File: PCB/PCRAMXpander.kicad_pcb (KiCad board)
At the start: 2 copper layers, 134.6 x 97.8 mm, 22 parts, among them J1 Bus_ISA_16bit, U1 ATF16V8B-15PU, U2 SN74LVCR16245ADGGR, U3 SN74LVC16244ADGGR, U4 SN74LVC16244ADGGR, U5 AS6C3216A-55TIN, U6 AS6C3216A-55TIN

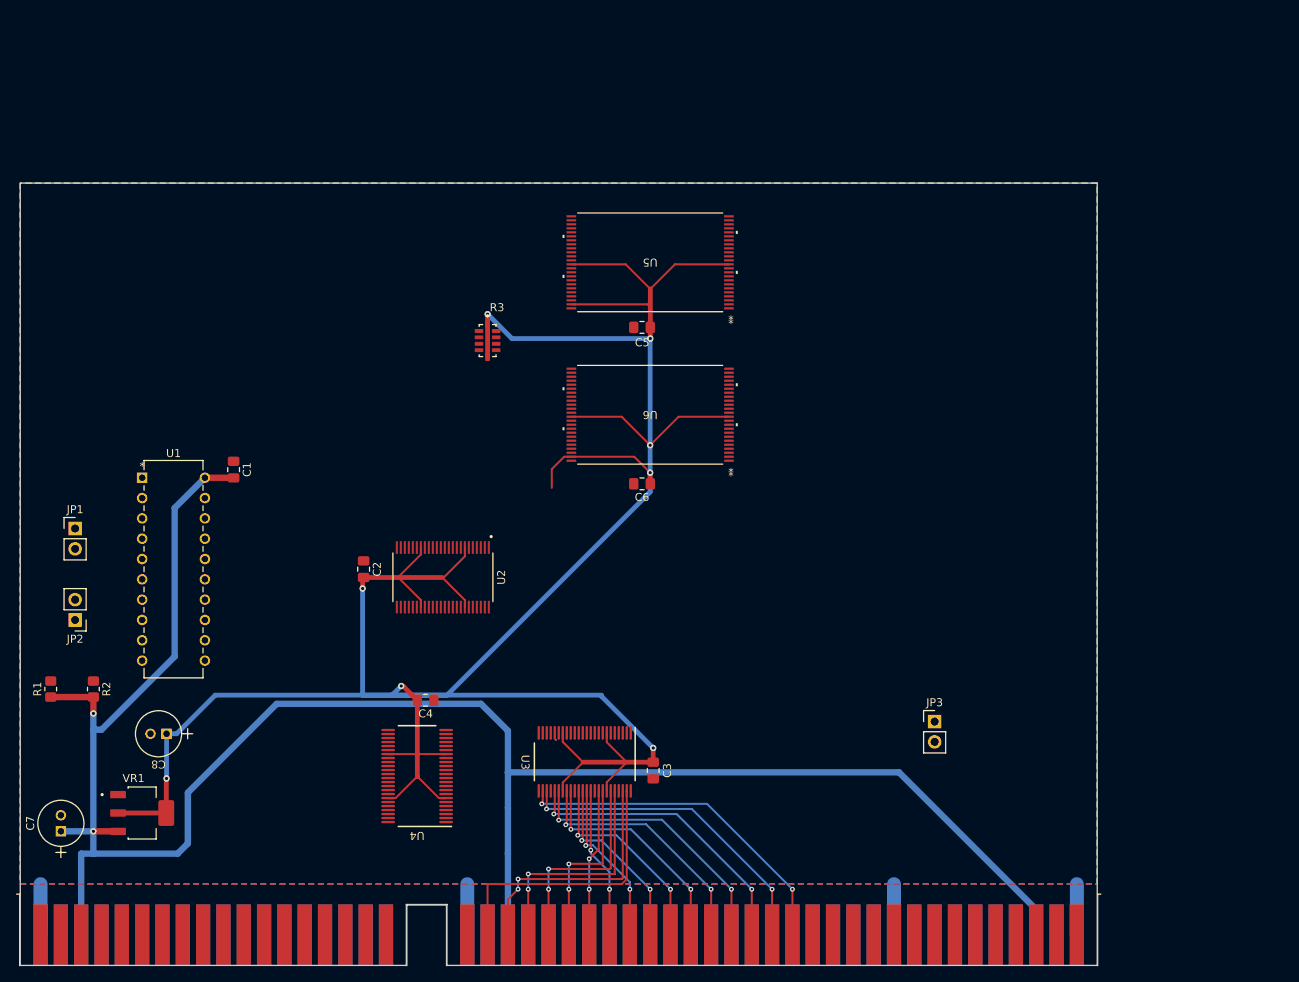
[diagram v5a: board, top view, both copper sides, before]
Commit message: More manual routing
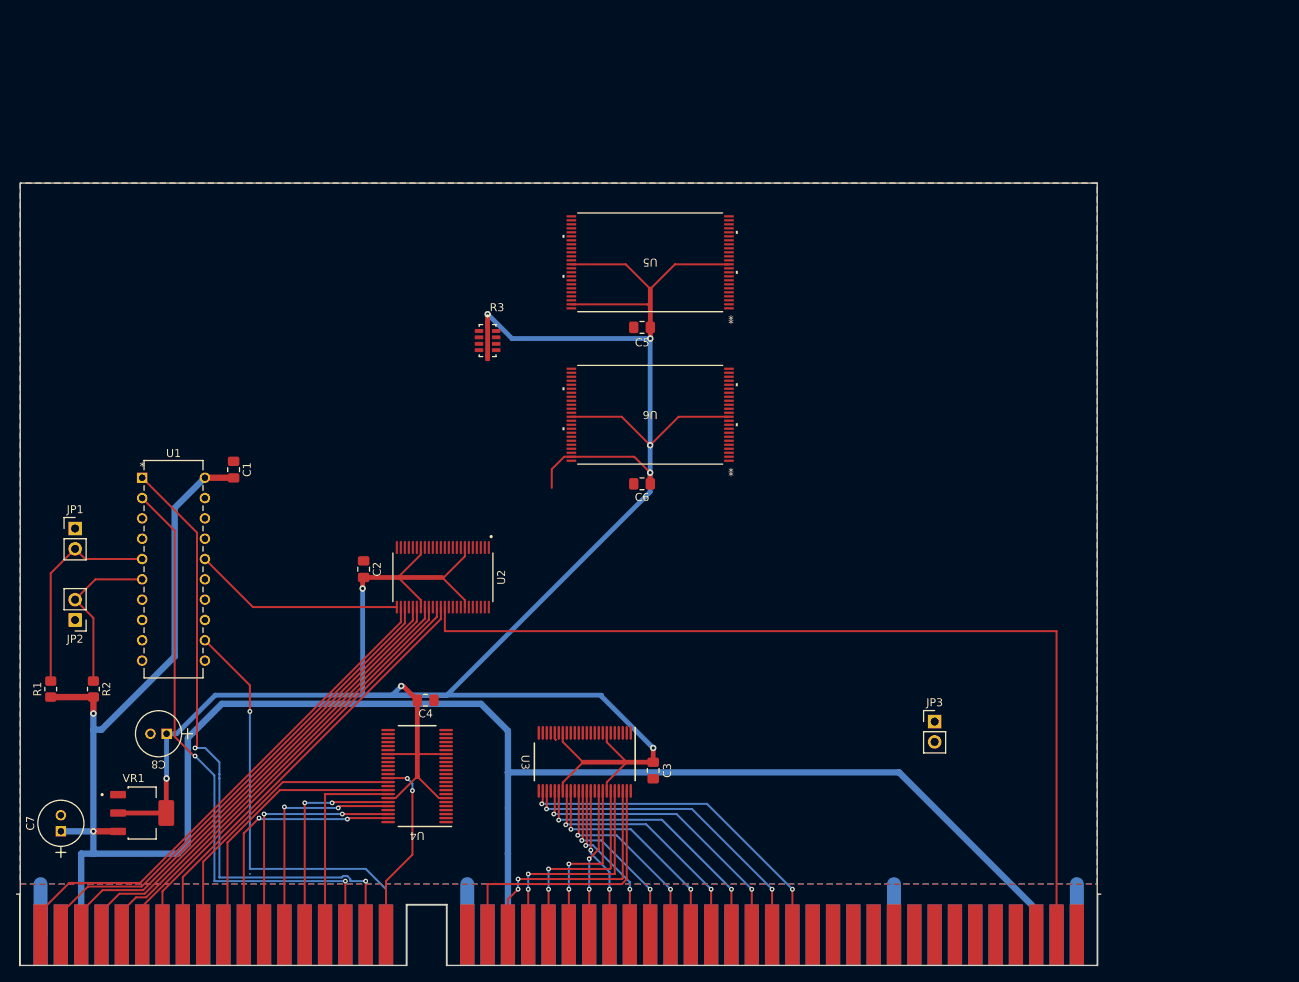
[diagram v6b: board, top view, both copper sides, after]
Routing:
- net Net-(J1-DB7): track 0.00 -> 117.4 mm
- net LA23: track 0.00 -> 80.4 mm, vias 0 -> 2
- net LA22: track 0.00 -> 74.8 mm, vias 0 -> 2
- net Net-(J1-D15): track 0.00 -> 64.8 mm
- net Net-(J1-D14): track 0.00 -> 62.7 mm
- net Net-(J1-D13): track 0.00 -> 61.1 mm
- net Net-(J1-D12): track 0.00 -> 59.2 mm
- net Net-(J1-D11): track 0.00 -> 57.4 mm
- net Net-(J1-D10): track 0.00 -> 55.8 mm
- net Net-(J1-D9): track 0.00 -> 55.2 mm
- net MEMCS16: track 0.00 -> 54.7 mm, vias 0 -> 1
- net Net-(J1-D8): track 0.00 -> 54.3 mm
- net MEMW: track 0.00 -> 36.4 mm
- net MEMR: track 0.00 -> 34.6 mm
- net LA17: track 0.00 -> 31.6 mm, vias 0 -> 2
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
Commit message: More manual routing
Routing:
- net Net-(J1-DB6): track 0.00 -> 114.6 mm, vias 0 -> 2
- net Net-(J1-DB5): track 0.00 -> 111.0 mm, vias 0 -> 2
- net Net-(J1-DB4): track 0.00 -> 107.8 mm, vias 0 -> 2
- net Net-(JP3-A): track 0.00 -> 105.3 mm, vias 0 -> 2
- net Net-(J1-DB3): track 0.00 -> 104.5 mm, vias 0 -> 2
- net Net-(J1-DB2): track 0.00 -> 101.2 mm, vias 0 -> 2
- net Net-(J1-DB0): track 0.00 -> 94.6 mm, vias 0 -> 2
- net Net-(J1-DB1): track 0.00 -> 93.3 mm, vias 0 -> 3
- net +3.3V: track 357.0 -> 351.5 mm

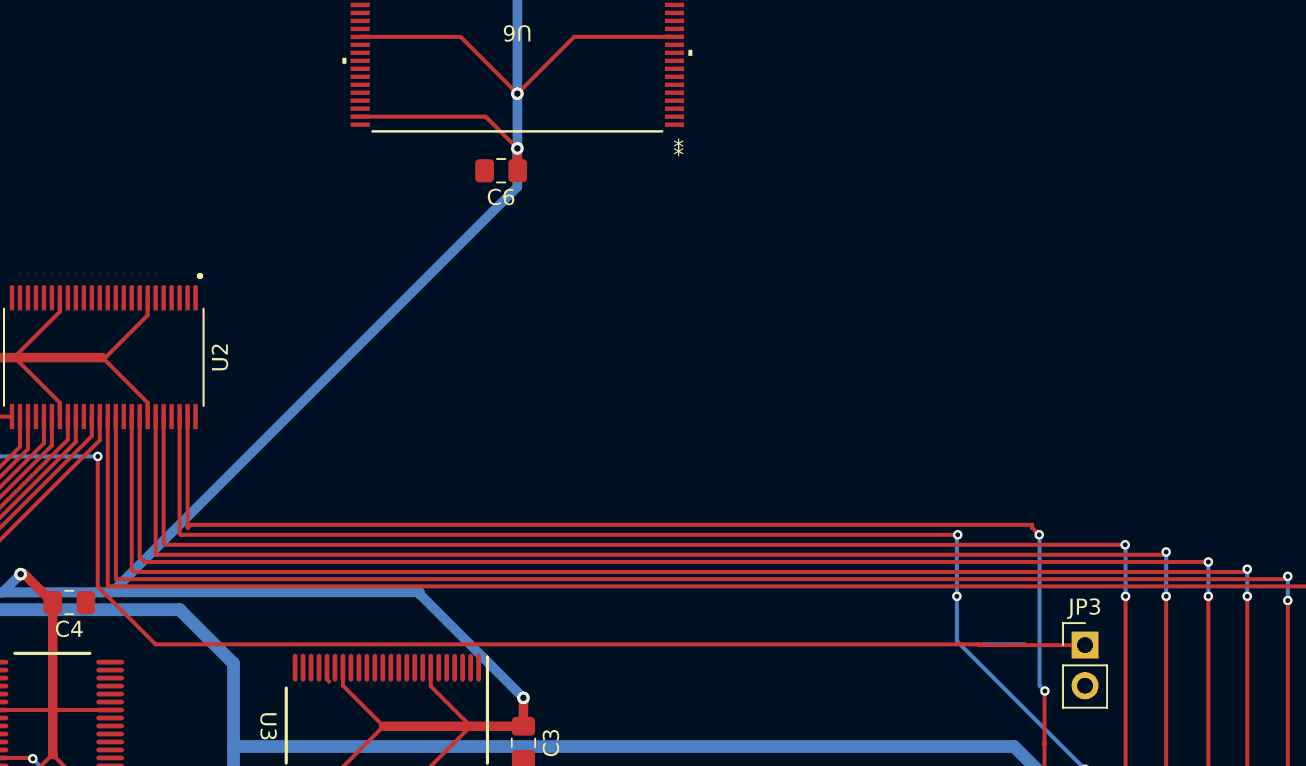
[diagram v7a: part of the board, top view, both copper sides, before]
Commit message: More manual routing
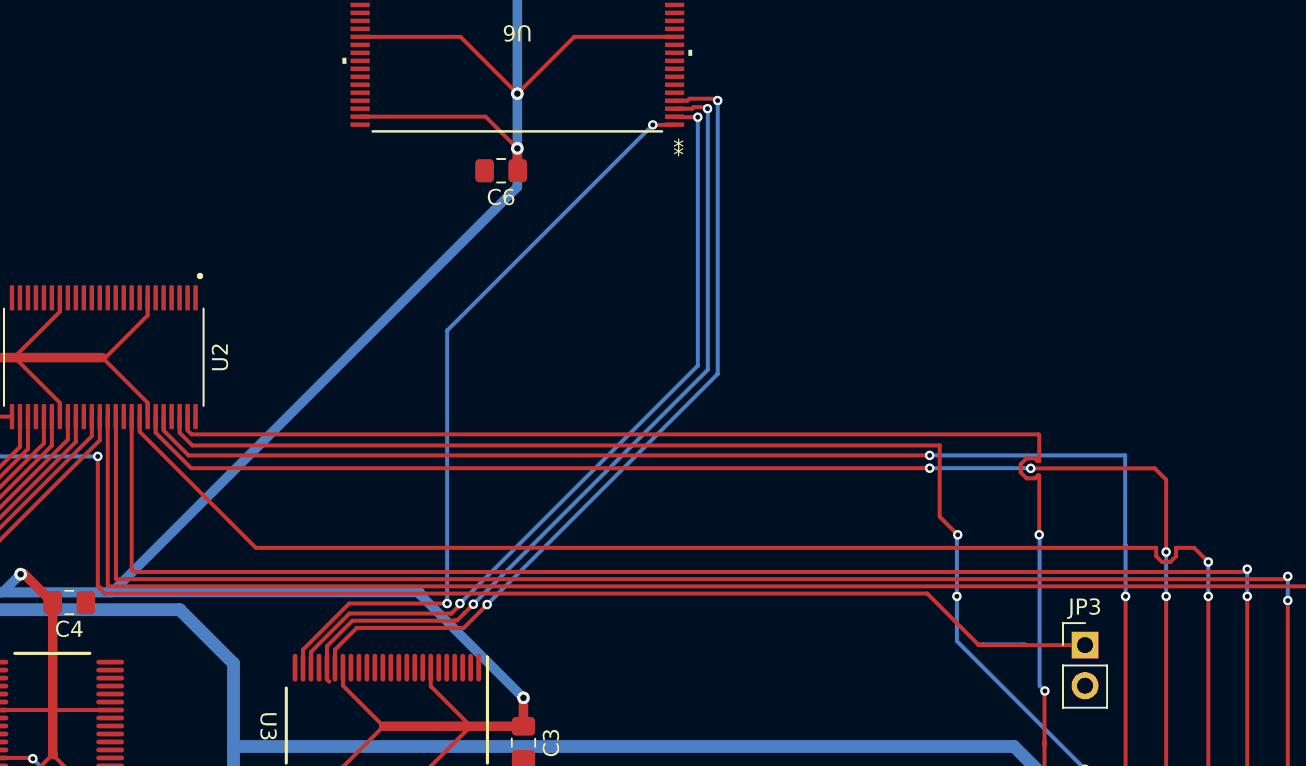
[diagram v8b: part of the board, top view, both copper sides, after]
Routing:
- net A12: track 0.00 -> 52.2 mm, vias 0 -> 2
- net A13: track 0.00 -> 50.9 mm, vias 0 -> 2
- net A14: track 0.00 -> 49.8 mm, vias 0 -> 2
- net A15: track 0.00 -> 48.0 mm, vias 0 -> 2
- net Net-(J1-DB4): track 107.8 -> 104.5 mm
- net Net-(J1-DB0): track 94.6 -> 96.9 mm
- net Net-(J1-DB3): track 104.5 -> 102.6 mm, vias 2 -> 4
- net Net-(J1-DB1): track 93.3 -> 92.2 mm
- net Net-(J1-DB2): track 101.2 -> 100.3 mm
